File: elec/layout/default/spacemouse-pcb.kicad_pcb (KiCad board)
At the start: 2 copper layers, 225.7 x 100.8 mm, 0 parts

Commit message: start
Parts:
- added ?: , , F.Cu at (166.0, 76.5)
- added ?: , , F.Cu at (108.0, 134.5)
- added ?: , , F.Cu at (108.0, 76.5)
- added ?: , , F.Cu at (166.0, 134.5)
- added A: , lib:CONN-TH_4P-P2.50_XH-4A, F.Cu at (154.8, 131.5)
- added B: , lib:CONN-TH_4P-P2.50_XH-4A, F.Cu at (108.5, 122.8)
- added C: , lib:CONN-TH_4P-P2.50_XH-4A, F.Cu at (154.8, 77.0)
- added D: , lib:CONN-TH_4P-P2.50_XH-4A, F.Cu at (165.5, 87.8)
- added U1: , lib:ProMicro, F.Cu at (122.9, 86.5)
- added U2: , lib:HDR-TH_12P-P2.54-V-M, F.Cu at (112.2, 86.4)
- added U3: , lib:HDR-TH_12P-P2.54-V-M, F.Cu at (133.5, 86.4)
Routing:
- added copper zone on B.Cu, net (none)
- added copper zone on F.Cu, net (none)
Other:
- board size 225.7 x 100.8 mm -> 78 x 78 mm
- board text removed: "{{GITHASH}}"

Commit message: basic complete
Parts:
- removed ? (x4): , 
- removed U2, U3: , lib:HDR-TH_12P-P2.54-V-M
- added C1: 50V 100nF X7R ±10% 1206 Multilayer Ceramic Capacitors MLCC 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, lib:C1206, F.Cu at (152.5, 129.5)
- added C2: 50V 100nF X7R ±10% 1206 Multilayer Ceramic Capacitors MLCC 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, lib:C1206, F.Cu at (119.5, 102.5)
- added C3: 50V 100nF X7R ±10% 1206 Multilayer Ceramic Capacitors MLCC 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, lib:C1206, F.Cu at (151.0, 70.0)
- added C4: 50V 100nF X7R ±10% 1206 Multilayer Ceramic Capacitors MLCC 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, lib:C1206, F.Cu at (179.5, 97.5)
- added H1: MountingHole_3.5mm, MountingHole:MountingHole_3.5mm, F.Cu at (120.5, 128.8)
- added H2: MountingHole_3.5mm, MountingHole:MountingHole_3.5mm, F.Cu at (120.5, 70.8)
- added H3: MountingHole_3.5mm, MountingHole:MountingHole_3.5mm, F.Cu at (178.5, 70.8)
- added H4: MountingHole_3.5mm, MountingHole:MountingHole_3.5mm, F.Cu at (178.5, 128.8)
- moved B 23.5 mm to (114.5, 100.0)
- moved D 22.6 mm to (184.5, 100.0)
- moved U1 15.2 mm to (136.9, 80.6)
- moved C 12.0 mm to (153.8, 65.0)
- moved A 5.62 mm to (150.0, 134.5)
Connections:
- A pad 3: joyA-_3 -> a1
- A pad 4: joyA-_4 -> a0
- B pad 3: joyB-_3 -> a3
- B pad 4: joyB-_4 -> a2
- C pad 3: joyC-_3 -> a7
- C pad 4: joyC-_4 -> a6
- D pad 3: joyD-_3 -> a9
- D pad 4: joyD-_4 -> a8
- U1 pad 11: (no net) -> a8
- U1 pad 12: (no net) -> a9
- U1 pad 17: (no net) -> a0
- U1 pad 18: (no net) -> a1
- U1 pad 19: (no net) -> a2
- U1 pad 20: (no net) -> a3
- U1 pad 7: (no net) -> a6
- U1 pad 9: (no net) -> a7
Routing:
- net vcc: track 0.00 -> 181.1 mm
- net gnd: track 0.00 -> 173.0 mm, vias 0 -> 1
- net a8: track 0.00 -> 63.4 mm
- net a9: track 0.00 -> 57.9 mm
- net a1: track 0.00 -> 54.3 mm
- net a0: track 0.00 -> 50.8 mm
- net a3: track 0.00 -> 42.6 mm
- net a7: track 0.00 -> 39.7 mm
- net a2: track 0.00 -> 37.1 mm
- net a6: track 0.00 -> 35.2 mm

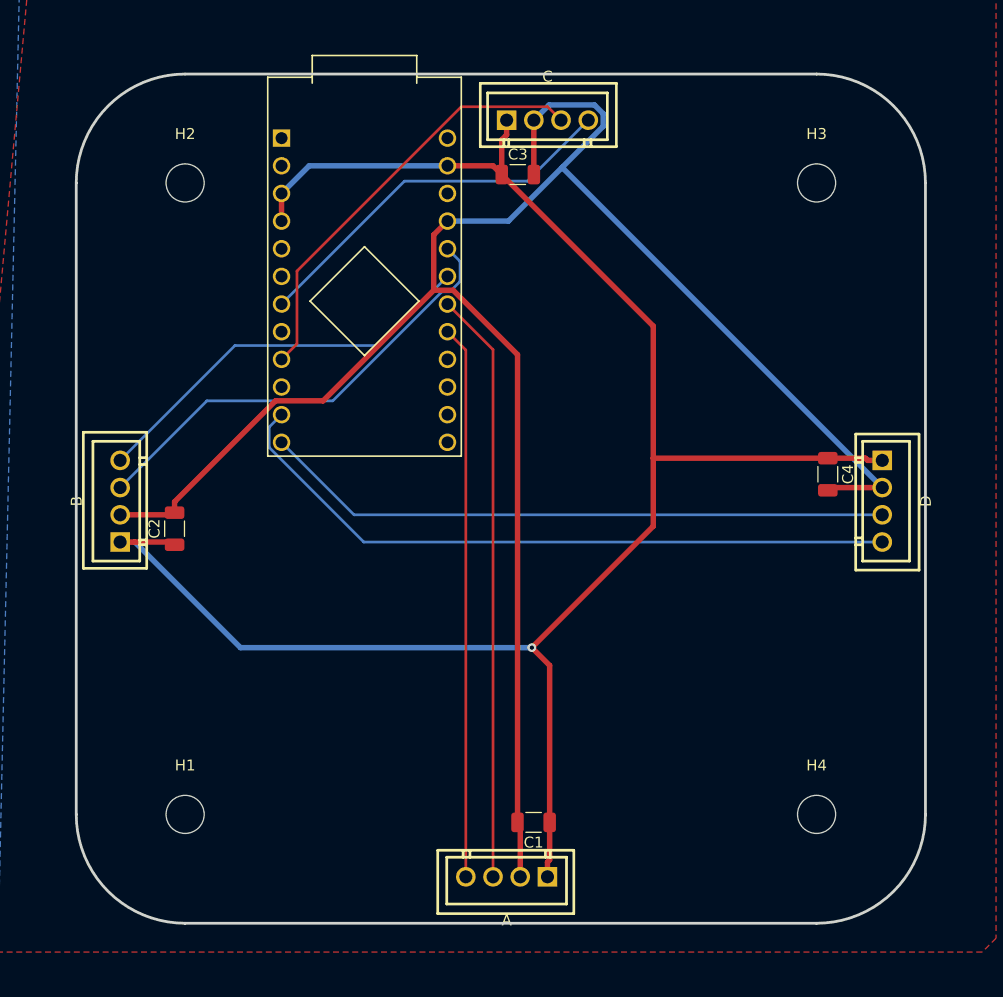
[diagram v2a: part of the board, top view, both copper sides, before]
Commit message: fix swapped XYs, cleaner labels
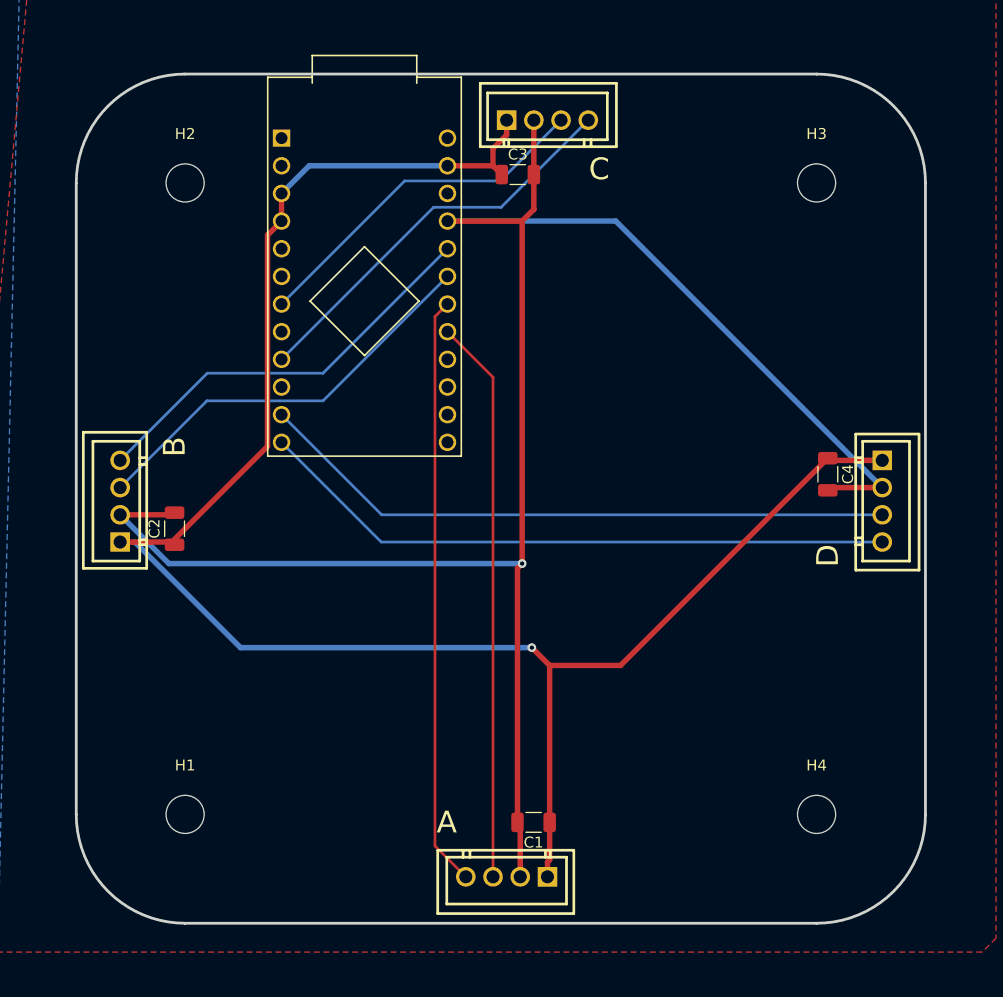
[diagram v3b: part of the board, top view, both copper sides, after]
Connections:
- A pad 3: a1 -> a0
- A pad 4: a0 -> a1
- B pad 3: a3 -> a2
- B pad 4: a2 -> a3
- C pad 3: a7 -> a6
- C pad 4: a6 -> a7
- D pad 3: a9 -> a8
- D pad 4: a8 -> a9
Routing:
- net vcc: track 181.1 -> 176.1 mm, vias 0 -> 1
- net a3: track 42.6 -> 38.1 mm
- net a8: track 63.4 -> 59.0 mm
- net gnd: track 173.0 -> 169.8 mm
- net a6: track 35.2 -> 32.7 mm
- net a7: track 39.7 -> 37.3 mm
- net a2: track 37.1 -> 38.1 mm
- net a9: track 57.9 -> 59.0 mm
- net a0: track 50.8 -> 51.8 mm
